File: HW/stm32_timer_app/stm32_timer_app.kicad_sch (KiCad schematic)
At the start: 68 parts, among them J1 105164-0001, J2 61300411121, J3 PH2-06-UA, J4 691213710002, J5 691213710002, Q1 BTA10-600BRG, U1 RT9193-33GB, U2 MOC3041SM, U3 STM32F103C8T6, Y1 ABL-8.000MHZ-B2, Y2 ABS25-32.768KHZ-6-4-T

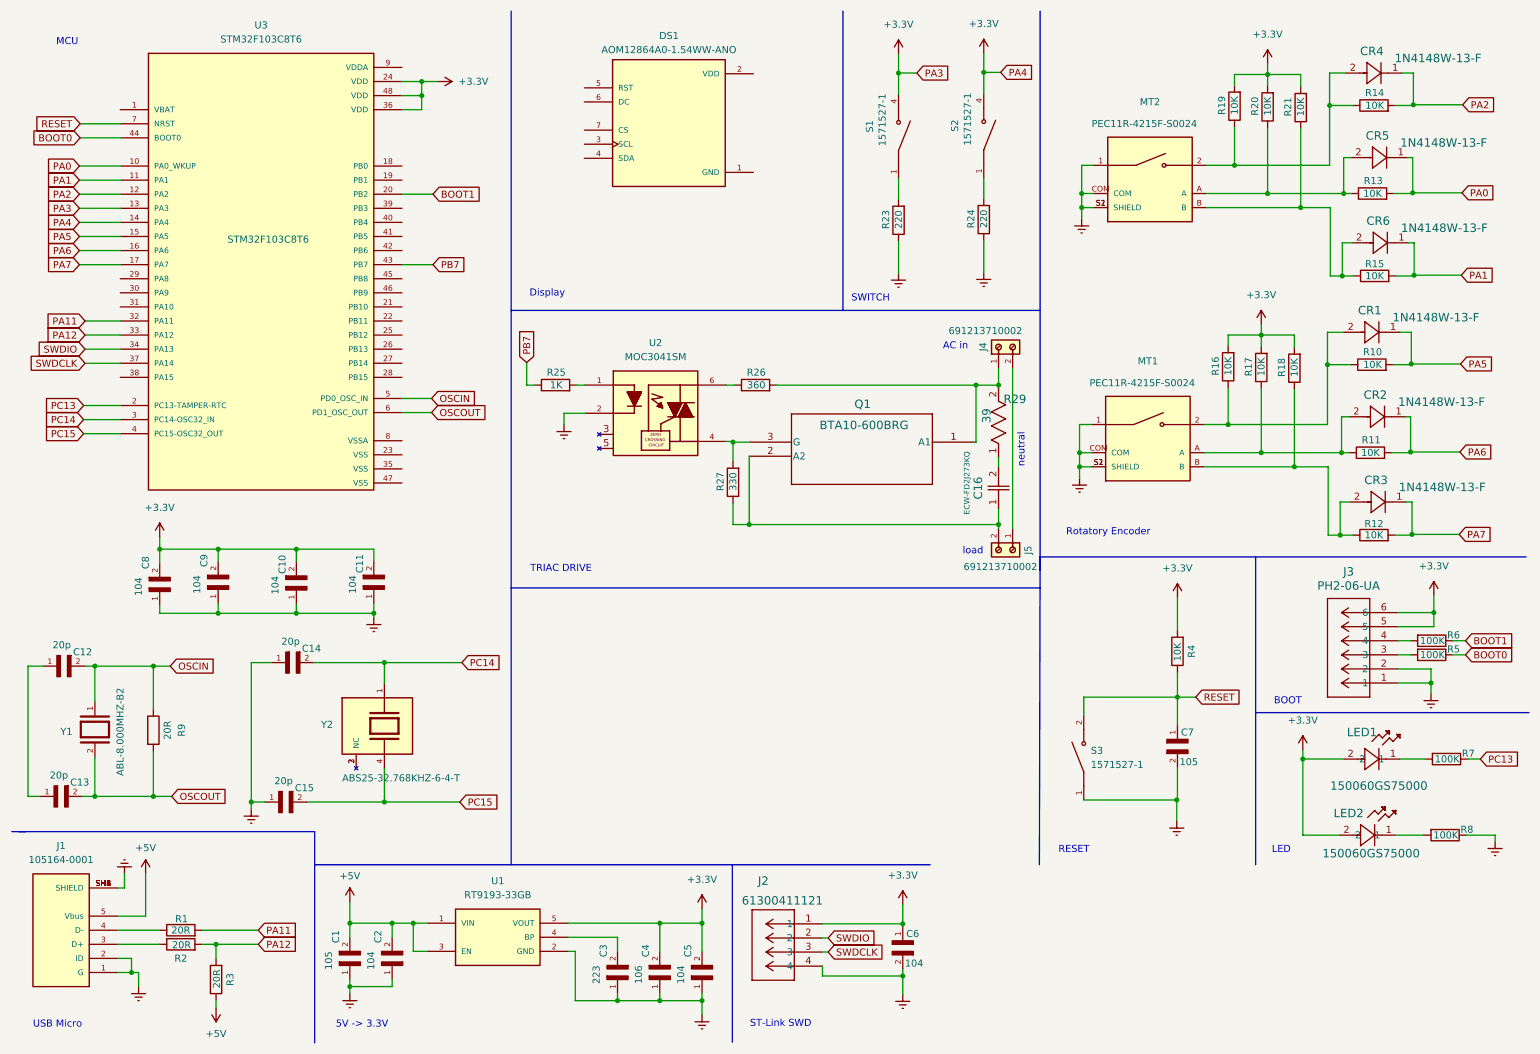
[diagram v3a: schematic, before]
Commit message: update schematic
update schematic and foot print / 3D body libraries
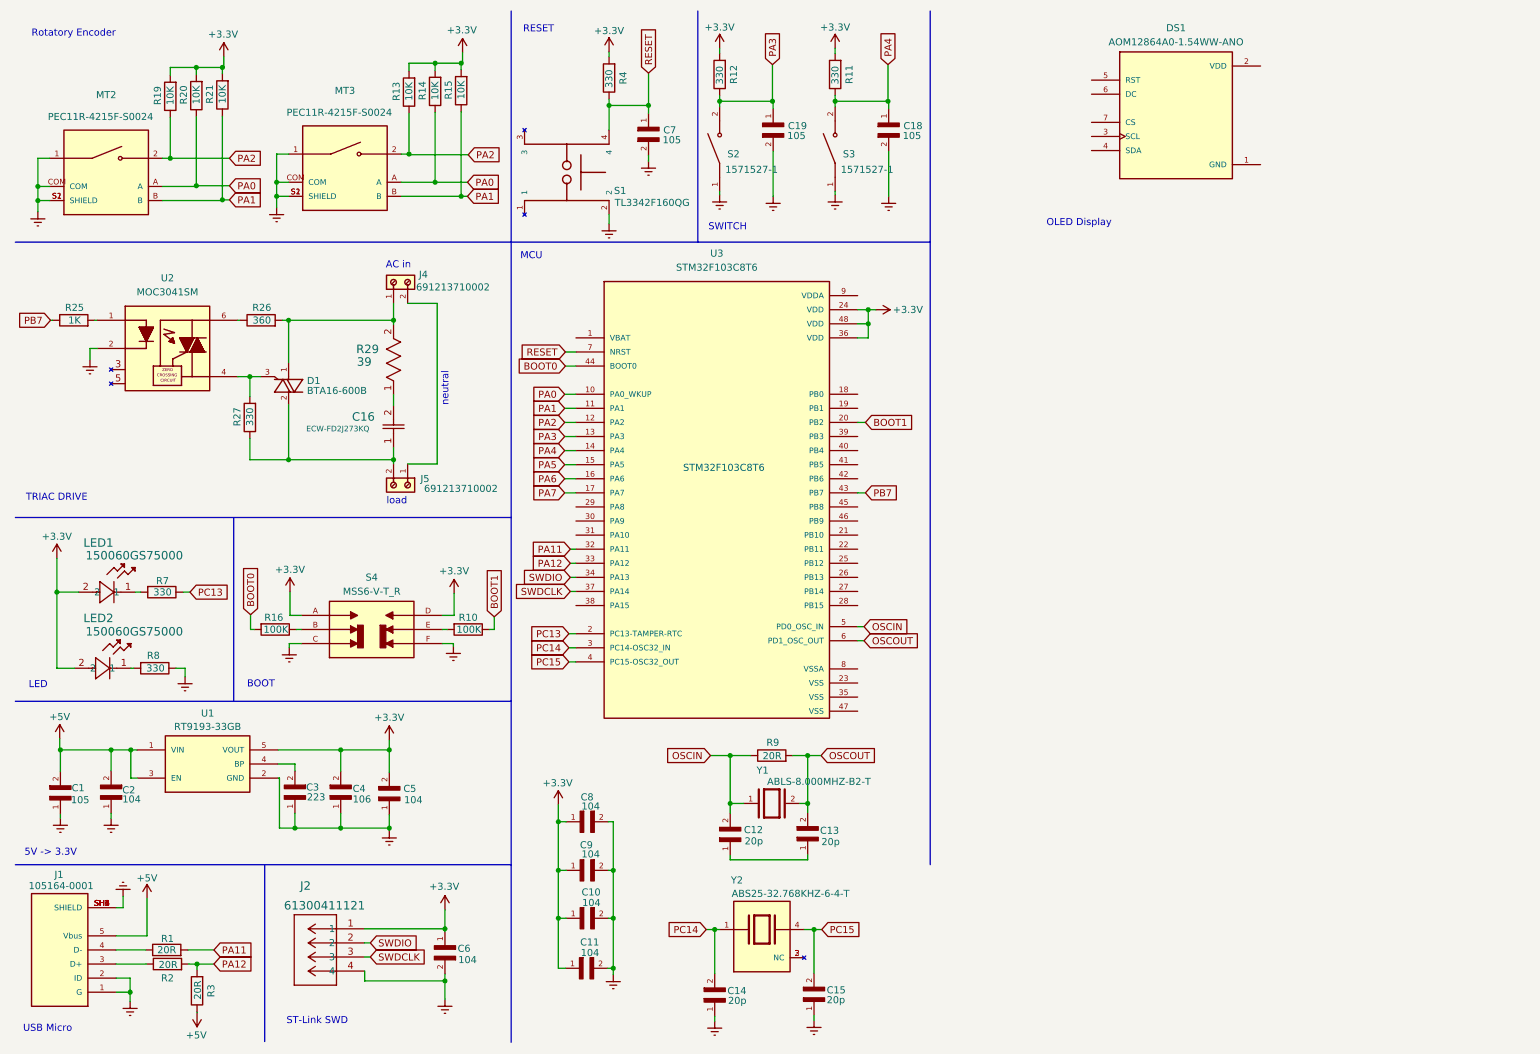
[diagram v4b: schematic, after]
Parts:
- removed CR1, CR2, CR3, CR4, CR5, CR6: 1N4148W-13-F, SOD123_DIO, symbol 1N4148W_13_F:1N4148W-13-F
- removed J3: PH2-06-UA, PH2_06_UA:CONN_PH2-06-UA_ADM, symbol CONN_PH2:PH2-06-UA
- removed MT1: PEC11R-4215F-S0024, PEC11R-4215F-S0024:XDCR_PEC11R-4215F-S0024, symbol PEC11R-4215F-S0024:PEC11R-4215F-S0024
- removed Q1: BTA10-600BRG, BTA10_600BRG:TO-220AB_STM, symbol 2023-12-12_16-02-27:BTA10-600BRG
- removed R17, R18: 10K, Resistor_SMD:R_0603_1608Metric, symbol Device:R
- removed R23, R24: 220, Resistor_SMD:R_0603_1608Metric, symbol Device:R
- removed R5, R6: 100K, Resistor_SMD:R_0603_1608Metric, symbol Device:R
- removed S1: 1571527-1, 1571527-1:SW_1571527-1, symbol 1571527-1:1571527-1
- removed Y1: ABL-8.000MHZ-B2, ABL-8.000MHZ-B2:XTAL_HC49P488W46L1150T500H350, symbol ABL-8.000MHZ-B2:ABL-8.000MHZ-B2
- added C18, C19: 105, LD03ZD475MAB2A:CAPC1608X90, symbol LD03ZD475MAB2A:LD03ZD475MAB2A
- added D1: BTA16-600B, BTA16-600B:TO255P1040X460X1975-3, symbol BTA16-600B:BTA16-600B
- added MT3: PEC11R-4215F-S0024, PEC11R-4215F-S0024:XDCR_PEC11R-4215F-S0024, symbol PEC11R-4215F-S0024:PEC11R-4215F-S0024
- added S1: TL3342F160QG, TL3342F160QG:SW_TL3342F160QG, symbol TL3342F160QG:TL3342F160QG
- added S4: MSS6-V-T_R, MSS6-V-T_R:SW_MSS6-V-T_R, symbol MSS6-V-T_R:MSS6-V-T_R
- added Y1: ABLS-8.000MHZ-B2-T, ABLS-8.000MHZ-B2-T:XTAL_ABLS-8.000MHZ-B2-T, symbol ABLS-8.000MHZ-B2-T:ABLS-8.000MHZ-B2-T
- R10, R16: value 10K -> 100K
- R11, R12, R4: value 10K -> 330
- R7, R8: value 100K -> 330
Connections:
- net +3.3V: now also C10.1, C11.1, C8.1, C9.1, R11.2, R12.2, R13.2, R14.2, R15.2, S4.A, S4.D; no longer C10.2, C11.2, C8.2, C9.2, R16.2, S2.3, S2.4, U3.13 (PA3), U3.14 (PA4)
- net BOOT0: now also R16.2
- net BOOT1: now also R10.1
- net OSCIN: now also Y1.1
- net OSCOUT: now also Y1.2
- net PA0: now also MT2.A, R14.1, R20.1, MT3.A; no longer R13.2
- net PA1: now also MT2.B, R15.1, R21.1, MT3.B; no longer R15.2
- net PA2: now also MT2.2, R13.1, R19.1, MT3.2; no longer R14.2
- net PA5: no longer R10.2
- net PA6: no longer R11.2
- net PA7: no longer R12.2
- net RESET: now also S1.4; no longer S3.2, S3.4
- net at J4.1, R26.2, R29.2: now also D1.1
- net at R27.2, U2.4: now also D1.3
- net at S2.1: now also S2.3; no longer S2.2
- net at C14.1: no longer C15.1
- net at C16.1, J5.2, R27.1: now also D1.2
- net at C1.1: no longer C2.1
- net PA3: now reaches R12.1
- net PA3: now also S2.2, S2.4, U3.13 (PA3), C19.1
- net at S3.1, S3.3: no longer C7.2
- net at R16.1: now also S4.B; no longer R10.1
- net PA4: now reaches R11.1
- net PA4: now also S3.2, S3.4, U3.14 (PA4), C18.1
- new net: C10.2, C11.2, C8.2, C9.2
- new net: MT3.1, MT3.COM, MT3.S1 (SHIELD), MT3.S2 (SHIELD)
- new net: R10.2, S4.E
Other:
- note added: "OLED Display"
- note removed: "Display"
- moved on the sheet: C1, C10, C11, C12, C13, C14, C15, C16, C2, C3, C4, C5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
